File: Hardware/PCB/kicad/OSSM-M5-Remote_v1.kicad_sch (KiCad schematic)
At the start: 26 parts, among them M5-CORE2 M5_CORE2, U1 PCA9685PW, U2 MCP23017_SS, U3 JST-PH-2MM,180

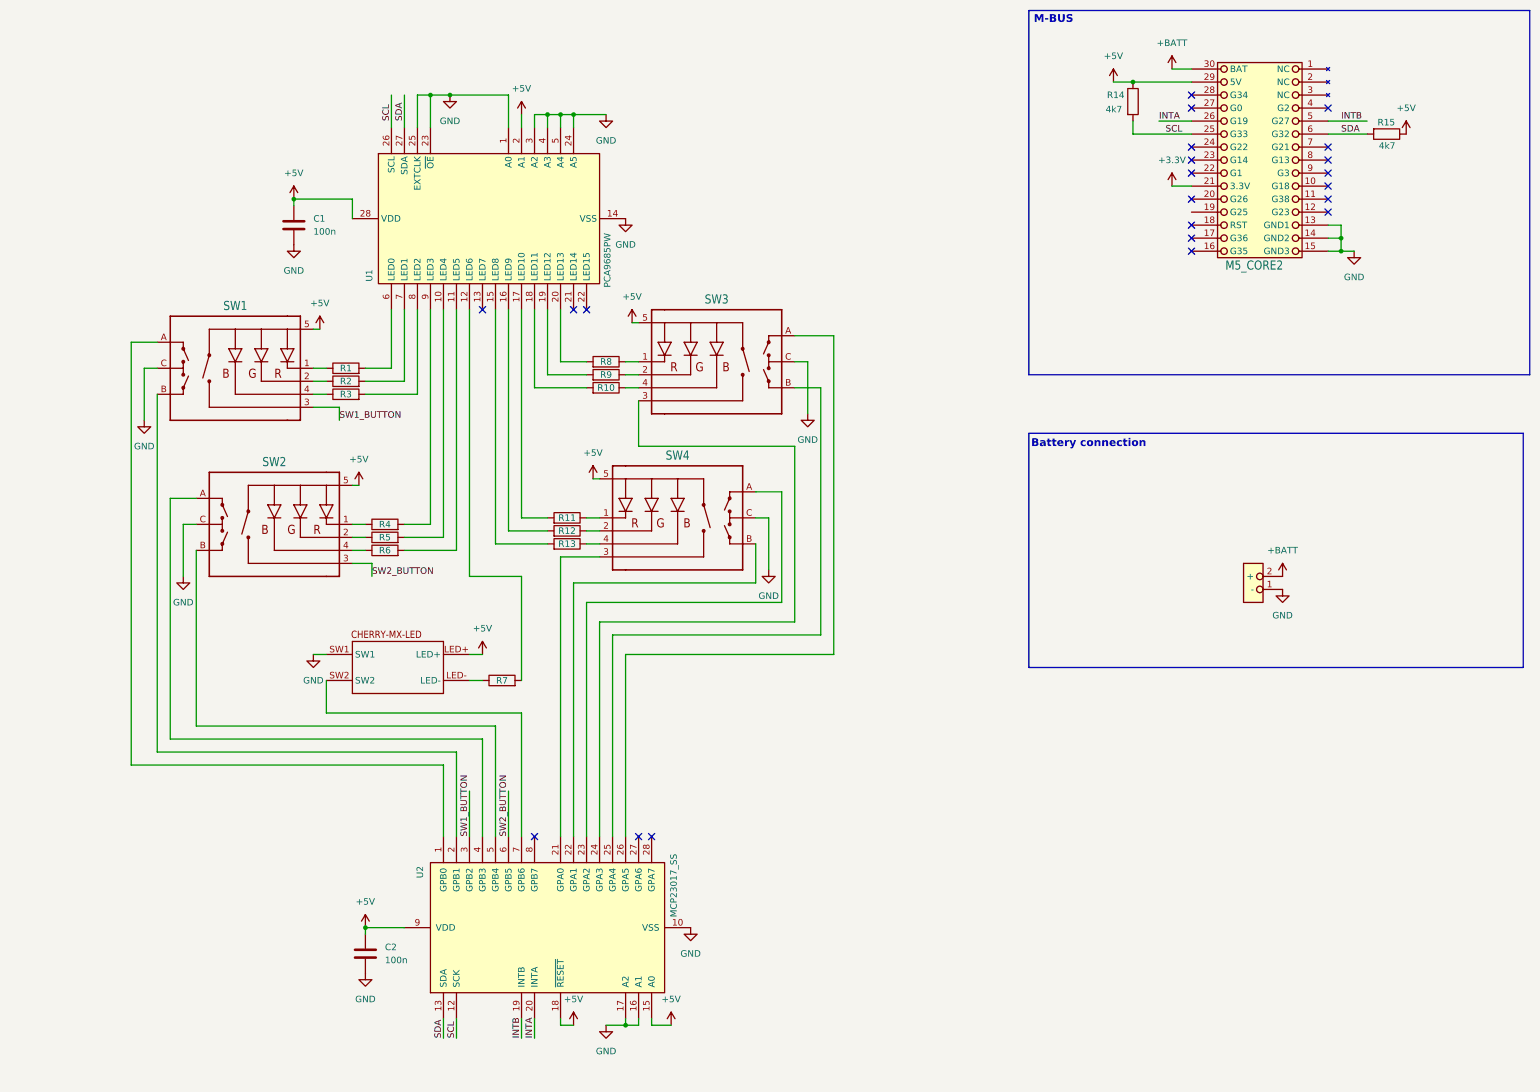
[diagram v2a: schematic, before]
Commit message: Cleaner schematic
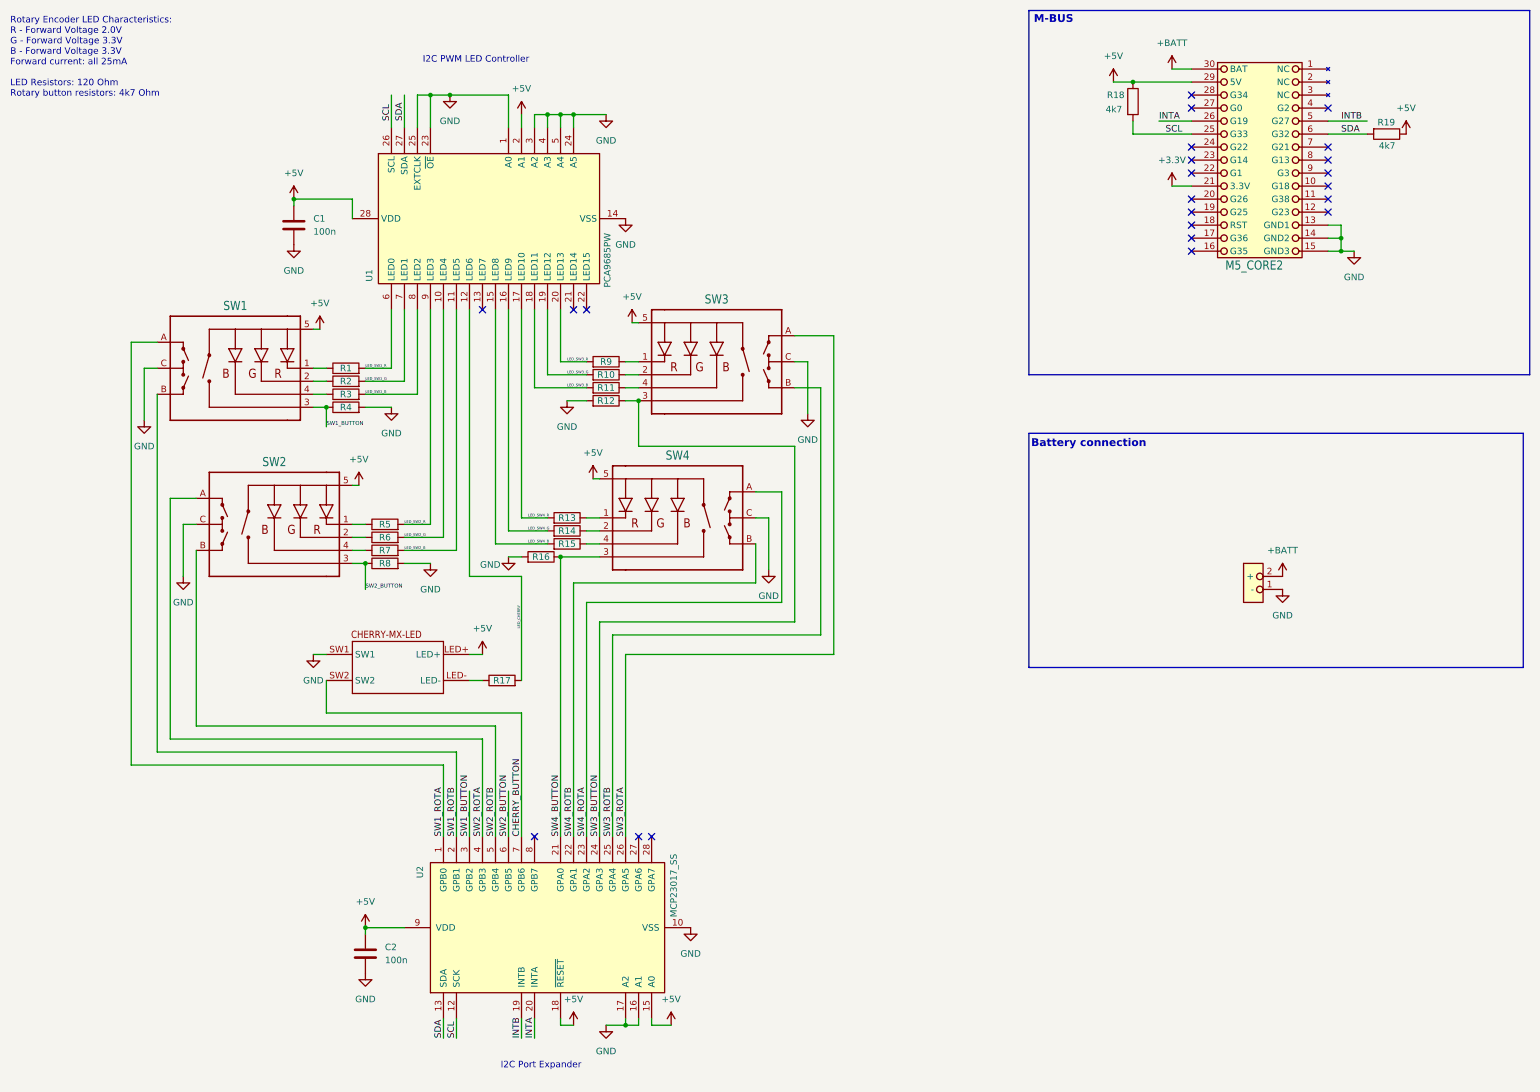
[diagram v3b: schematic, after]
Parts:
- added R12, R16, R4, R8: 4k7, Resistor_SMD:R_0603_1608Metric, symbol Device:R
- C1, C2: footprint (none) -> Capacitor_SMD:C_0402_1005Metric; JLCPCB Part Number (none) -> C1525; MFR Part Number (none) -> CL05B104KO5NNNC; Manufacturer (none) -> https://datasheet.lcsc.com/lcsc/2304140030_Samsung-Electro-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
- R1, R2, R3: value 220 -> 120R; footprint (none) -> Resistor_SMD:R_0603_1608Metric; JLCPCB Part Number (none) -> C22787; MFR Part Number (none) -> 0603WAF1200T5E; Manufacturer (none) -> UNI-ROYAL
- R10: renamed from R9; value 220 -> 120R; footprint (none) -> Resistor_SMD:R_0603_1608Metric; JLCPCB Part Number (none) -> C22787; MFR Part Number (none) -> 0603WAF1200T5E; Manufacturer (none) -> UNI-ROYAL
- R11: renamed from R10; value 220 -> 120R; footprint (none) -> Resistor_SMD:R_0603_1608Metric; JLCPCB Part Number (none) -> C22787; MFR Part Number (none) -> 0603WAF1200T5E; Manufacturer (none) -> UNI-ROYAL
- R13: renamed from R11; value 220 -> 120R; footprint (none) -> Resistor_SMD:R_0603_1608Metric; JLCPCB Part Number (none) -> C22787; MFR Part Number (none) -> 0603WAF1200T5E; Manufacturer (none) -> UNI-ROYAL
- R14: renamed from R12; value 220 -> 120R; footprint (none) -> Resistor_SMD:R_0603_1608Metric; JLCPCB Part Number (none) -> C22787; MFR Part Number (none) -> 0603WAF1200T5E; Manufacturer (none) -> UNI-ROYAL
- R15: renamed from R13; value 220 -> 120R; footprint (none) -> Resistor_SMD:R_0603_1608Metric; JLCPCB Part Number (none) -> C22787; MFR Part Number (none) -> 0603WAF1200T5E; Manufacturer (none) -> UNI-ROYAL
- R17: renamed from R7; value 220 -> 120R; footprint (none) -> Resistor_SMD:R_0603_1608Metric; JLCPCB Part Number (none) -> C22787; MFR Part Number (none) -> 0603WAF1200T5E; Manufacturer (none) -> UNI-ROYAL
- R18: renamed from R14; footprint (none) -> Resistor_SMD:R_0603_1608Metric; JLCPCB Part Number (none) -> C23162; MFR Part Number (none) -> 0603WAF4701T5E; Manufacturer (none) -> UNI-ROYAL
- R19: renamed from R15; footprint (none) -> Resistor_SMD:R_0603_1608Metric; JLCPCB Part Number (none) -> C23162; MFR Part Number (none) -> 0603WAF4701T5E; Manufacturer (none) -> UNI-ROYAL
- R5: renamed from R4; value 220 -> 120R; footprint (none) -> Resistor_SMD:R_0603_1608Metric; JLCPCB Part Number (none) -> C22787; MFR Part Number (none) -> 0603WAF1200T5E; Manufacturer (none) -> UNI-ROYAL
- R6: renamed from R5; value 220 -> 120R; footprint (none) -> Resistor_SMD:R_0603_1608Metric; JLCPCB Part Number (none) -> C22787; MFR Part Number (none) -> 0603WAF1200T5E; Manufacturer (none) -> UNI-ROYAL
- R7: renamed from R6; value 220 -> 120R; footprint (none) -> Resistor_SMD:R_0603_1608Metric; JLCPCB Part Number (none) -> C22787; MFR Part Number (none) -> 0603WAF1200T5E; Manufacturer (none) -> UNI-ROYAL
- R9: renamed from R8; value 220 -> 120R; footprint (none) -> Resistor_SMD:R_0603_1608Metric; JLCPCB Part Number (none) -> C22787; MFR Part Number (none) -> 0603WAF1200T5E; Manufacturer (none) -> UNI-ROYAL
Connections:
- net GND: now also R12.2, R16.2, R4.2, R8.2
- net SW1_BUTTON: now also R4.1
- net SW2_BUTTON: now also R8.1
- net LED_SW4_G: now reaches R14.2, U1.16 (LED9)
- net LED_SW1_G: now reaches R2.2, U1.7 (LED1)
- net SW2_ROTA: now reaches SW2.A, U2.4 (GPB3)
- net SW2_ROTB: now reaches SW2.B, U2.5 (GPB4)
- net LED_SW4_R: now reaches R13.2, U1.17 (LED10)
- net SW1_ROTA: now reaches SW1.A, U2.1 (GPB0)
- net SW1_ROTB: now reaches SW1.B, U2.2 (GPB1)
- net SW4_BUTTON: now reaches SW4.3 (SW), U2.21 (GPA0)
- net SW4_BUTTON: now also R16.1
- net SW4_ROTA: now reaches SW4.A, U2.23 (GPA2)
- net SW4_ROTB: now reaches SW4.B, U2.22 (GPA1)
- net LED_SW3_G: now reaches R10.2, U1.19 (LED12)
- net LED_SW2_G: now reaches R6.2, U1.10 (LED4)
- net LED_SW2_B: now reaches R7.2, U1.11 (LED5)
- net LED_CHERRY: now reaches R17.2, U1.12 (LED6)
- net LED_SW4_B: now reaches R15.2, U1.15 (LED8)
- net LED_SW3_B: now reaches R11.2, U1.18 (LED11)
- net LED_SW3_R: now reaches R9.2, U1.20 (LED13)
- net LED_SW1_R: now reaches R1.2, U1.6 (LED0)
- net LED_SW1_B: now reaches R3.2, U1.8 (LED2)
- net LED_SW2_R: now reaches R5.2, U1.9 (LED3)
- net SW3_BUTTON: now reaches SW3.3 (SW), U2.24 (GPA3)
- net SW3_BUTTON: now also R12.1
- net SW3_ROTB: now reaches SW3.B, U2.25 (GPA4)
- net SW3_ROTA: now reaches SW3.A, U2.26 (GPA5)
- net CHERRY_BUTTON: now reaches U$4.SW2, U2.7 (GPB6)
- no-connect marks 22 -> 23
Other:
- note added: "I2C PWM LED Controller"
- note added: "I2C Port Expander"
- note added: "Rotary Encoder LED Characteristics: R - Forward Voltage 2.0V G - Forward Voltage 3.3V B - Forward Voltage 3.3V Forward current: all 25mA LED Resistors: 120 Ohm Rotary button resistors: 4k7 Ohm"

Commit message: Starting routing
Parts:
- added H1, H2, H3, H4: MountingHole, OSSM-M5-Remote_v1:mounting_hole_3.3mm, symbol Mechanical:MountingHole
- renumbered U$4 to U4
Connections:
- net GND: now also SW1.MH1, SW1.MH2, SW2.MH1, SW2.MH2, SW3.MH1, SW3.MH2, SW4.MH1, SW4.MH2
- net INTA: now also M5-CORE2.5 (G27); no longer M5-CORE2.26 (G19)
- net INTB: now also M5-CORE2.26 (G19); no longer M5-CORE2.5 (G27)
- net LED_SW3_B: now also U1.20 (LED13); no longer U1.18 (LED11)
- net LED_SW3_R: now also U1.18 (LED11); no longer U1.20 (LED13)
- net LED_SW4_B: now also U1.17 (LED10); no longer U1.15 (LED8)
- net LED_SW4_R: now also U1.15 (LED8); no longer U1.17 (LED10)
- net SW2_ROTA: now also SW2.B; no longer SW2.A
- net SW2_ROTB: now also SW2.A; no longer SW2.B
- net SW3_ROTA: now also SW3.B; no longer SW3.A
- net SW3_ROTB: now also SW3.A; no longer SW3.B
- net LEDD_SW4_G: now reaches R14.1, SW4.2 (-G)
- net LEDD_SW1_G: now reaches R2.1, SW1.2 (-G)
- net LEDD_SW2_R: now reaches R5.1, SW2.1 (-R)
- net LEDD_SW2_G: now reaches R6.1, SW2.2 (-G)
- net LEDD_SW2_B: now reaches R7.1, SW2.4 (-B)
- net LEDD_SW4_R: now reaches R13.1, SW4.1 (-R)
- net LEDD_SW1_R: now reaches R1.1, SW1.1 (-R)
- net LEDD_SW1_B: now reaches R3.1, SW1.4 (-B)
- net LEDD_SW4_B: now reaches R15.1, SW4.4 (-B)
- net LEDD_SW3_G: now reaches R10.1, SW3.2 (-G)
- net LEDD_SW3_B: now reaches R11.1, SW3.4 (-B)
- net LEDD_SW3_R: now reaches R9.1, SW3.1 (-R)
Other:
- note added: "Mounting holes"

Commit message: Everything connected
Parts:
- R1, R10, R11, R13, R14, R15, R17, R2, R3, R5, R6, R7, R9: footprint Resistor_SMD:R_0603_1608Metric -> Resistor_SMD:R_1206_3216Metric; JLCPCB Part Number C22787 -> C17909
- R12, R16, R18, R19, R4, R8: footprint Resistor_SMD:R_0603_1608Metric -> Resistor_SMD:R_1206_3216Metric; JLCPCB Part Number C23162 -> C17936
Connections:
- net SW3_BUTTON: now also U2.26 (GPA5); no longer U2.24 (GPA3)
- net SW3_ROTA: now also SW3.A, U2.24 (GPA3); no longer SW3.B, U2.26 (GPA5)
- net SW3_ROTB: now also SW3.B; no longer SW3.A

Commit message: PCB updates
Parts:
- added B2: ~, Connector_JST:JST_PH_S2B-PH-K_1x02_P2.00mm_Horizontal, symbol OSSM-M5-Remote_v1-eagle-import:JST-PH-2MM,180,reversepolarity
- B1: renamed from U3; footprint OSSM-M5-Remote_v1:JST-PH-2.0MM_180DEGREES -> Connector_JST:JST_PH_S2B-PH-K_1x02_P2.00mm_Horizontal
- C1, C2: JLCPCB Part Number C1525 -> (none); LCSC Part # (none) -> C1525; Manufacturer https://datasheet.lcsc.com/lcsc/2304140030_Samsung-Electro-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 -> Samsung
- H1, H2, H3, H4: now not fitted
- M5-CORE2: MFR Part Number (none) -> 10129381-930001BLF; Manufacturer (none) -> Amphenol FCI
- R1, R10, R11, R13, R14, R15, R17, R2, R3, R5, R6, R7, R9: JLCPCB Part Number C17909 -> (none); LCSC Part # (none) -> C17909; MFR Part Number 0603WAF1200T5E -> 1206W4F1200T5E
- R12, R16, R18, R19, R4, R8: JLCPCB Part Number C17936 -> (none); LCSC Part # (none) -> C17936; MFR Part Number 0603WAF4701T5E -> 1206W4F4701T5E
- SW1, SW2, SW3, SW4: MFR Part Number (none) -> PEL12T4225SS1024; Manufacturer (none) -> Bourns
- U1: LCSC Part # (none) -> C2678753; MFR Part Number (none) -> PCA9685; Manufacturer (none) -> NXP
- U2: LCSC Part # (none) -> C506653; MFR Part Number (none) -> MCP23017-E/SS; Manufacturer (none) -> Microchip Tech
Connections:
- net +BATT: now also B2.1 (+)
- net GND: now also B2.2 (-)
- net LEDD_CHERRY: now reaches R17.1, U4.LED-
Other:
- note added: "I2C Address 0x21"
- note added: "I2C Address 0x42"
- note added: "Two possible battery polarities - populate only one connector on board"
- moved on the sheet: R17
